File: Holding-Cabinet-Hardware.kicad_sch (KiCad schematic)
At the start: 0 parts

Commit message: Added display circuit
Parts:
- added J1: Conn_02x19_Odd_Even, Connector_PinSocket_2.54mm:PinSocket_2x38_P2.54mm_Vertical, symbol Connector_Generic:Conn_02x19_Odd_Even
- added Q1, Q2, Q3, Q4, Q5, Q6, Q7, Q8: 2N3904, Package_TO_SOT_THT:TO-92_Inline, symbol Transistor_BJT:2N3904
- added Q10, Q11, Q12, Q9: AO3401A, Package_TO_SOT_SMD:SOT-23, symbol Transistor_FET:AO3401A
- added R1, R10, R11, R12, R13, R14, R15, R16, R17, R18, R19, R2, R20, R21, R22, R23, R24, R3, R4, R5, R6, R7, R8, R9: R_US, symbol Device:R_US
- added U1: CC56-12EWA, Display_7Segment:CA56-12EWA, symbol Display_Character:CC56-12EWA
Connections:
- new net: Q1.3 (C), R3.1
- new net: R3.2, U1.11 (a)
- new net: Q10.1 (G), R20.2, R23.1
- new net: Q10.2 (S), U1.6 (CC4)
- new net: Q12.1 (G), R22.1, R24.2
- new net: Q12.2 (S), U1.9 (CC2)
- new net: J1.14 (Pin_14), R18.2
- new net: J1.16 (Pin_16), R22.2
- new net: J1.18 (Pin_18), R21.2
- new net: J1.20 (Pin_20), R23.2
- new net: J1.22 (Pin_22), R1.1
- new net: J1.24 (Pin_24), R2.1
- new net: J1.26 (Pin_26), R5.2
- new net: J1.28 (Pin_28), R7.2
- new net: J1.30 (Pin_30), R9.2
- new net: J1.32 (Pin_32), R11.2
- new net: J1.34 (Pin_34), R13.2
- new net: J1.36 (Pin_36), R15.2
- new net: Q3.2 (B), R5.1
- new net: Q3.3 (C), R6.1
- new net: Q9.1 (G), R17.2, R18.1
- new net: Q8.2 (B), R15.1
- new net: Q9.2 (S), U1.12 (CC1)
- new net: Q7.2 (B), R13.1
- new net: Q7.3 (C), R14.1
- new net: R6.2, U1.4 (c)
- new net: Q4.2 (B), R7.1
- new net: Q4.3 (C), R8.1
- new net: R8.2, U1.2 (d)
- new net: Q5.3 (C), R10.1
- new net: R10.2, U1.1 (e)
- new net: Q11.1 (G), R19.2, R21.1
- new net: Q6.2 (B), R11.1
- new net: Q2.2 (B), R2.2
- new net: Q6.3 (C), R12.1
- new net: Q8.3 (C), R16.1
- new net: Q11.2 (S), U1.8 (CC3)
- new net: R12.2, U1.10 (f)
- new net: R16.2, U1.3 (DPX)
- new net: R14.2, U1.5 (g)
- new net: R4.2, U1.7 (b)
- new net: Q1.2 (B), R1.2
- new net: Q5.2 (B), R9.1
- new net: Q2.3 (C), R4.1
- new net GND: J1.37 (Pin_37), J1.38 (Pin_38), Q1.1 (E), Q2.1 (E), Q3.1 (E), Q4.1 (E), Q5.1 (E), Q6.1 (E), Q7.1 (E), Q8.1 (E)
- new net VCC: J1.1 (Pin_1), J1.2 (Pin_2), Q10.3 (D), Q9.3 (D), R17.1, R19.1, R20.1, R24.1

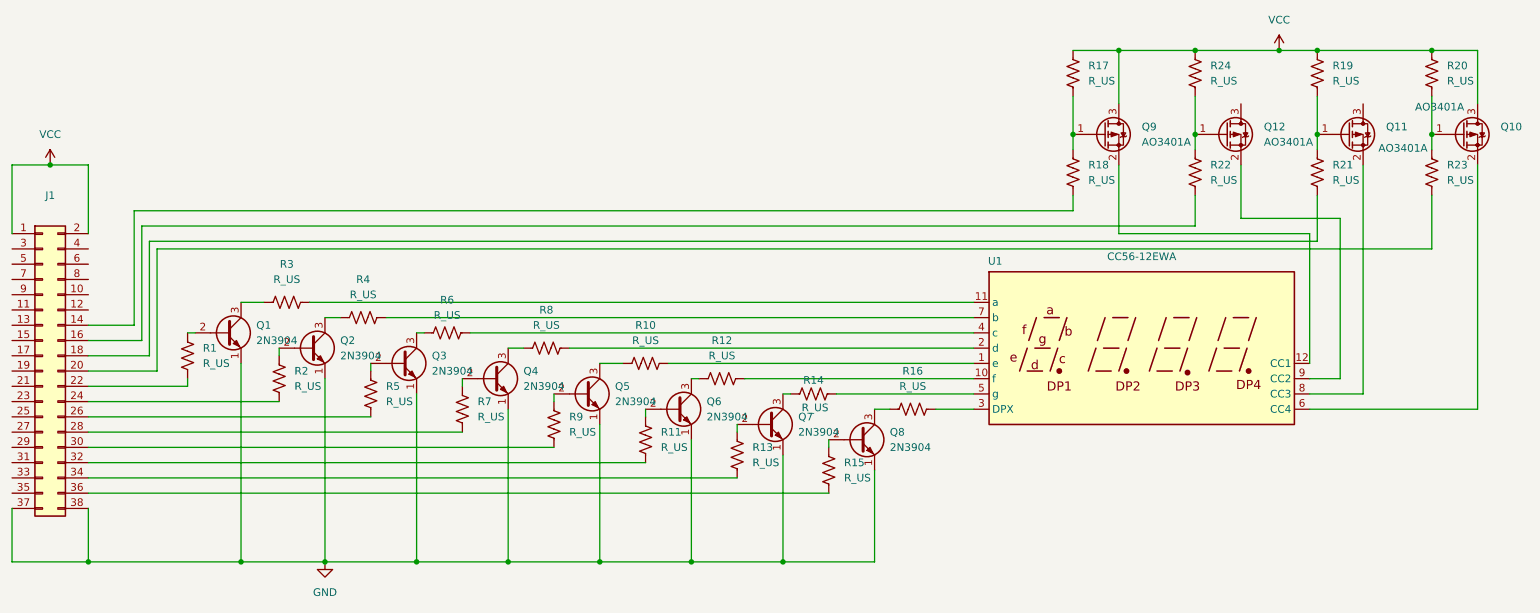
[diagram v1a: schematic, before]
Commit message: Created hierarchical sheet symbols on root sheet. Added the following schematics: Display, Power Supply, Heater, Fan, Sensing, Connectivity
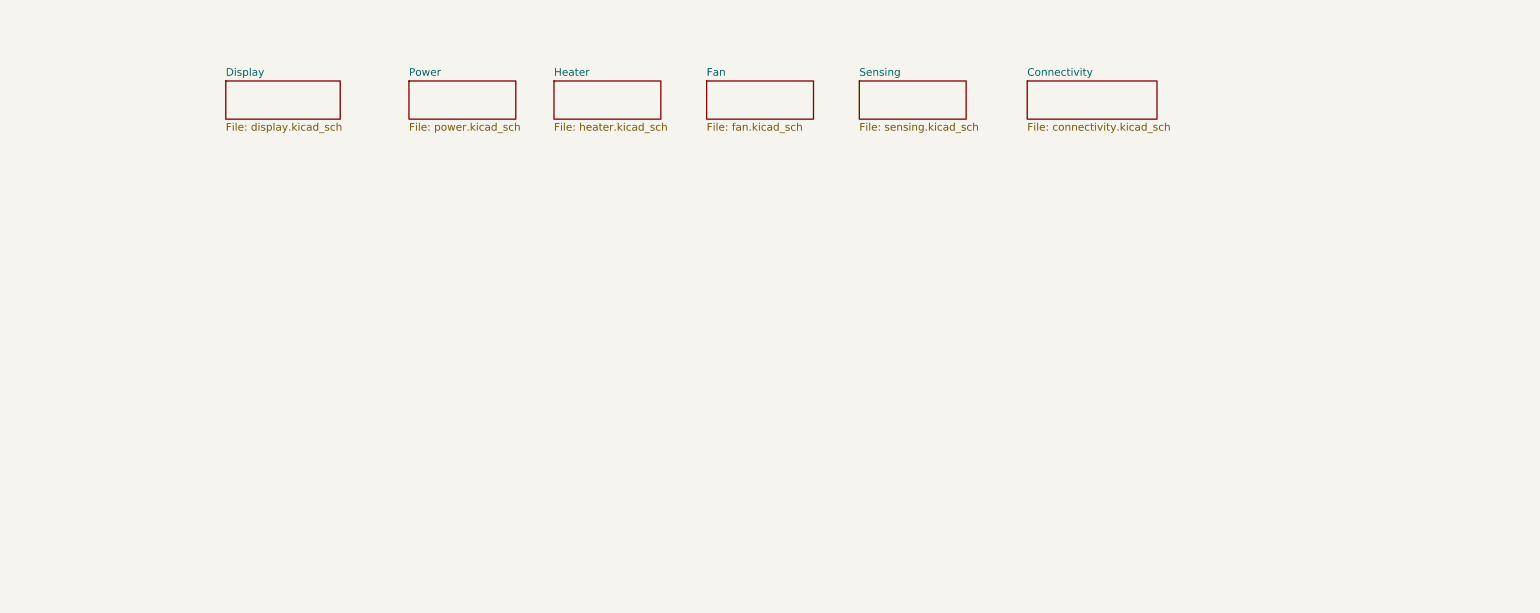
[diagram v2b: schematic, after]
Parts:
- removed J1: Conn_02x19_Odd_Even, Connector_PinSocket_2.54mm:PinSocket_2x38_P2.54mm_Vertical, symbol Connector_Generic:Conn_02x19_Odd_Even
- removed Q1, Q2, Q3, Q4, Q5, Q6, Q7, Q8: 2N3904, Package_TO_SOT_THT:TO-92_Inline, symbol Transistor_BJT:2N3904
- removed Q10, Q11, Q12, Q9: AO3401A, Package_TO_SOT_SMD:SOT-23, symbol Transistor_FET:AO3401A
- removed R1, R10, R11, R12, R13, R14, R15, R16, R17, R18, R19, R2, R20, R21, R22, R23, R24, R3, R4, R5, R6, R7, R8, R9: R_US, symbol Device:R_US
- removed U1: CC56-12EWA, Display_7Segment:CA56-12EWA, symbol Display_Character:CC56-12EWA
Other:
- added sheet Connectivity (connectivity.kicad_sch)
- added sheet Display (display.kicad_sch)
- added sheet Fan (fan.kicad_sch)
- added sheet Heater (heater.kicad_sch)
- added sheet Power (power.kicad_sch)
- added sheet Sensing (sensing.kicad_sch)
- title: Holding Cabinet -> Top Level Sheet 1 of [ ]

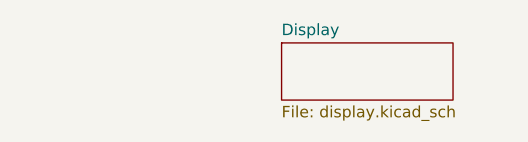
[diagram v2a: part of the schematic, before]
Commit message: Updated the root sheet and added the mcu schematic.
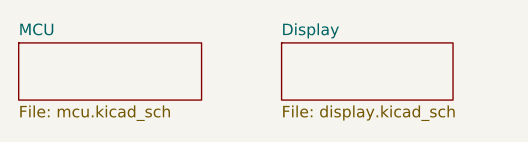
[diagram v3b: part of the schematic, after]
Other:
- added sheet MCU (mcu.kicad_sch)
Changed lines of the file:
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@@
+	)
+	(sheet
+		(at 27.94 58.42)
+		(size 20.32 6.35)
+		(exclude_from_sim no)
+		(in_bom yes)
+		(on_board yes)
+		(dnp no)
+		(fields_autoplaced yes)
+		(stroke
+			(width 0.1524)
+			(type solid)
+		)
+		(fill
+			(color 0 0 0 0)
+		)
+		(property "Sheetname" "MCU"
+			(at 27.94 57.7084 0)
+			(show_name no)
+			(do_not_autoplace no)
+			(effects
+				(font
+					(size 1.27 1.27)
+				)
+				(justify left bottom)
+			)
+		)
+		(property "Sheetfile" "mcu.kicad_sch"
+			(at 27.94 65.3546 0)
+			(show_name no)
+			(do_not_autoplace no)
+			(effects
+				(font
+					(size 1.27 1.27)
+				)
+				(justify left top)
+			)
+		)
+		(instances
+			(project "Holding-Cabinet-Hardware"
+				(path "/a7f4af77-1a94-4795-9d88-0a73c264962c"
+					(page "8")
+				)
+			)
+		)
 	)
 	(sheet

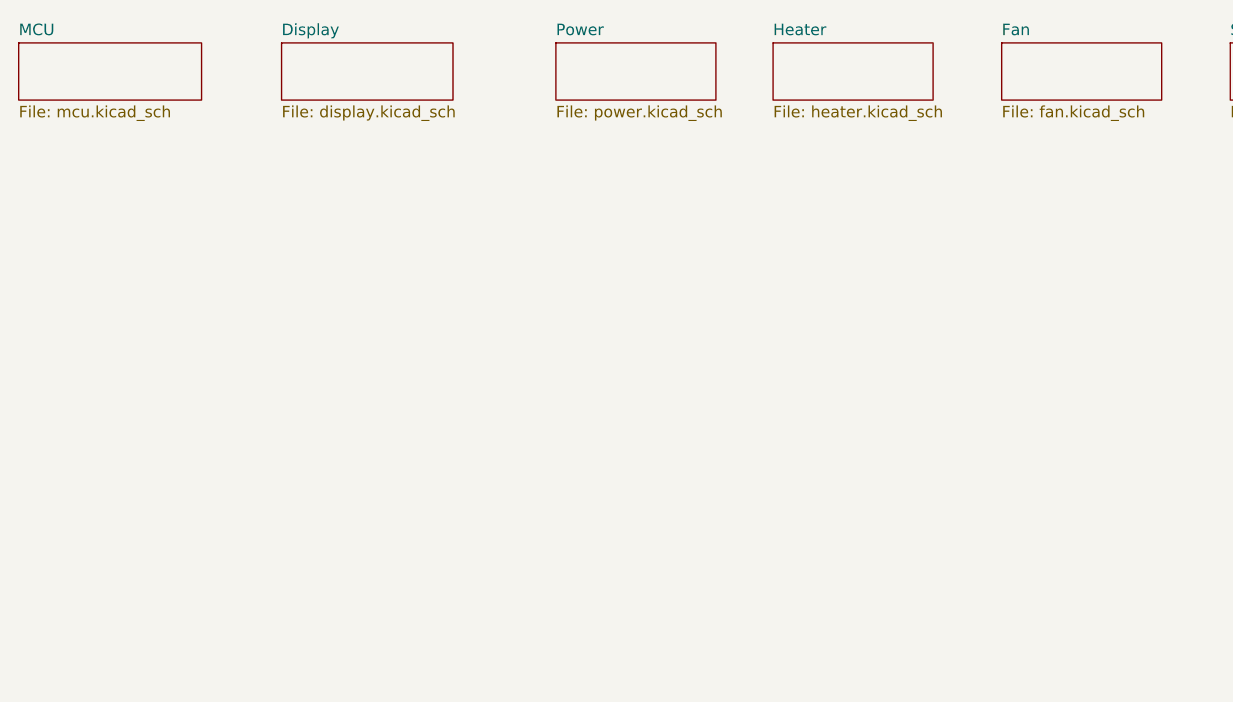
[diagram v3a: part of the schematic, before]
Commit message: Updated sheet connections for MCU to Display
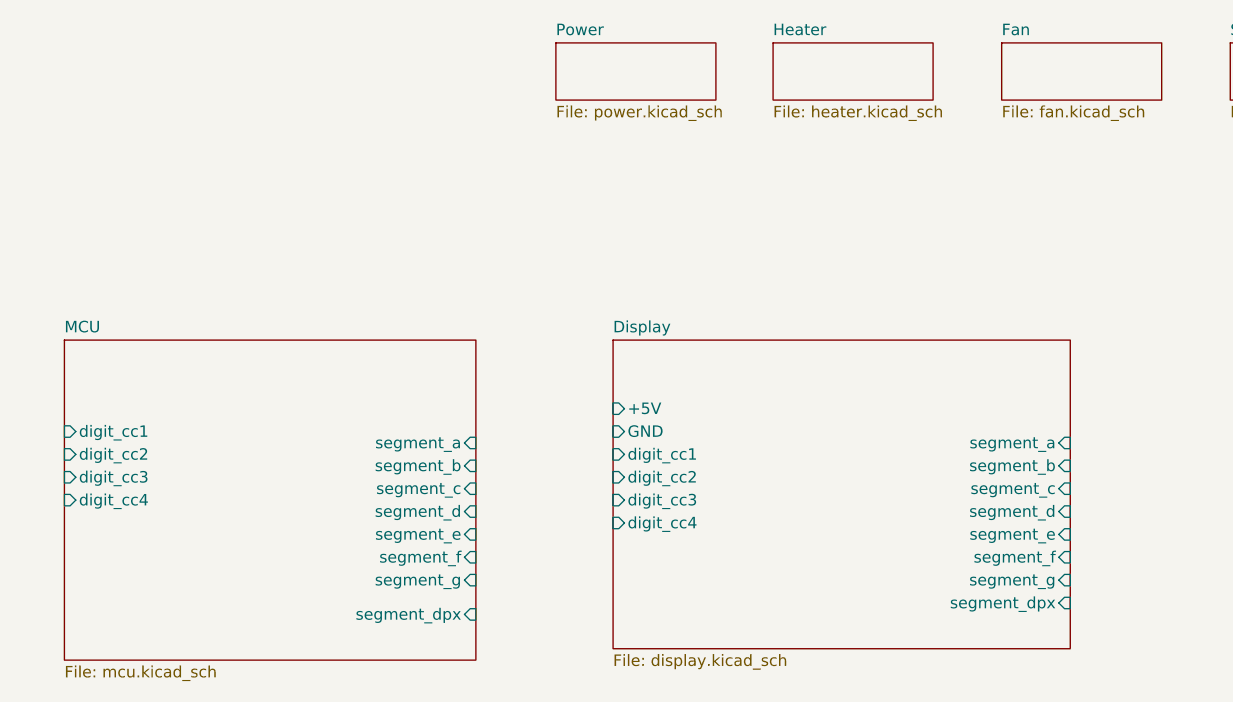
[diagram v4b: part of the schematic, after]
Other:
- sheet Display ports: added +5V, GND, digit_cc1, digit_cc2, digit_cc3, digit_cc4, segment_a, segment_b, segment_c, segment_d, segment_dpx, segment_e, segment_f, segment_g; removed none
- sheet MCU ports: added digit_cc1, digit_cc2, digit_cc3, digit_cc4, segment_a, segment_b, segment_c, segment_d, segment_dpx, segment_e, segment_f, segment_g; removed none

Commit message: Added an LCD
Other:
- sheet Display renamed 7-Segment Display
- added sheet LCD 16x2 Display (lcd_16_2_display.kicad_sch)
- sheet 7-Segment Display: file display.kicad_sch -> 7_segment_display.kicad_sch
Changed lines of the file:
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@@
 			(color 0 0 0 0)
 		)
-		(property "Sheetname" "Display"
+		(property "Sheetname" "7-Segment Display"
 			(at 93.98 90.7284 0)
 			(show_name no)
@@
 			)
 		)
-		(property "Sheetfile" "display.kicad_sch"
+		(property "Sheetfile" "7_segment_display.kicad_sch"
 			(at 93.98 126.3146 0)
 			(show_name no)
@@
 				)
 			)
+		)
+	)
+	(sheet
+		(at 158.75 91.44)
+		(size 57.15 34.29)
+		(exclude_from_sim no)
+		(in_bom yes)
+		(on_board yes)
+		(dnp no)
+		(fields_autoplaced yes)
+		(stroke
+			(width 0.1524)
+			(type solid)
+		)
+		(fill
+			(color 0 0 0 0)
+		)
+		(property "Sheetname" "LCD 16x2 Display"
+			(at 158.75 90.7284 0)
+			(show_name no)
+			(do_not_autoplace no)
+			(effects
+				(font
+					(size 1.27 1.27)
+				)
+				(justify left bottom)
+			)
+		)
+		(property "Sheetfile" "lcd_16_2_display.kicad_sch"
+			(at 158.75 126.3146 0)
+			(show_name no)
+			(do_not_autoplace no)
+			(effects
+				(font
+					(size 1.27 1.27)
+				)
+				(justify left top)
+			)
+		)
+		(instances
+			(project "Holding-Cabinet-Hardware"
+				(path "/a7f4af77-1a94-4795-9d88-0a73c264962c"
+					(page "9")
+				)
+			)

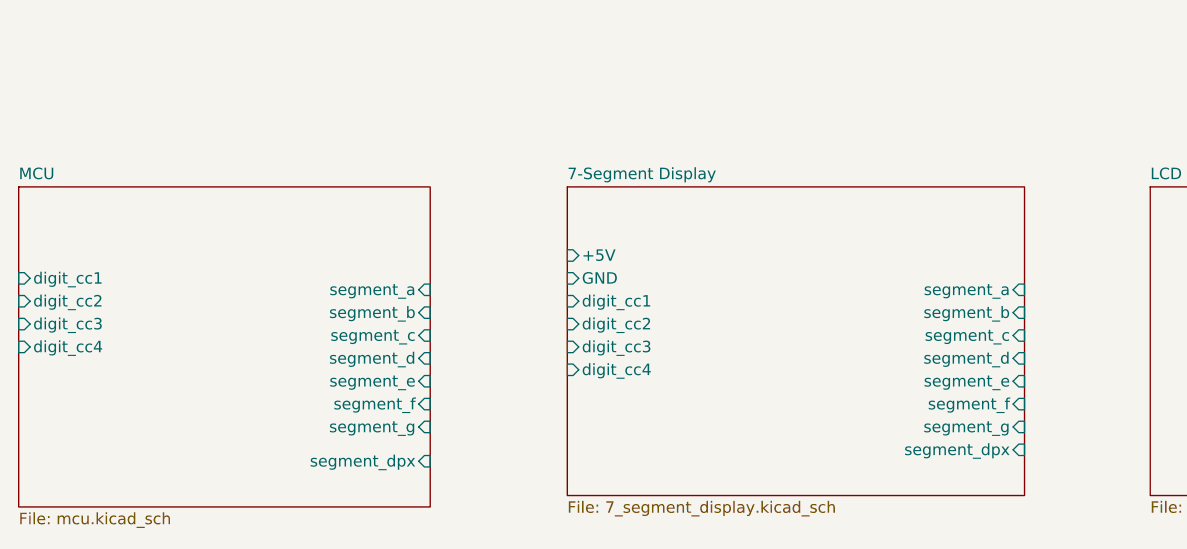
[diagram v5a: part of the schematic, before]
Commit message: Removed the 7 seg display
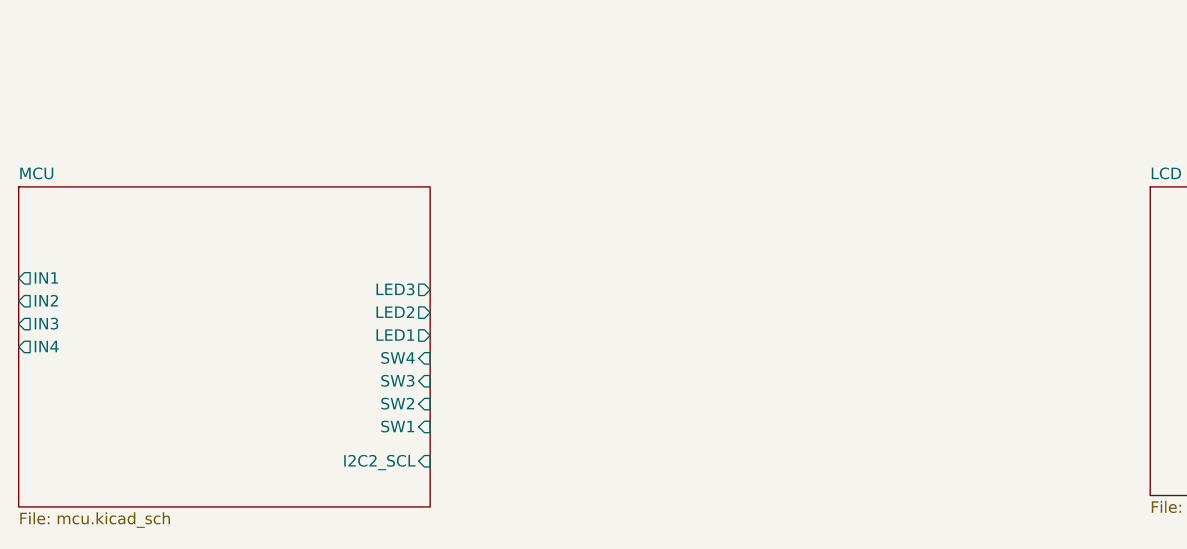
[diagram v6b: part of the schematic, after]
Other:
- removed sheet 7-Segment Display
- sheet MCU ports: added I2C2_SCL, IN1, IN2, IN3, IN4, LED1, LED2, LED3, SW1, SW2, SW3, SW4; removed digit_cc1, digit_cc2, digit_cc3, digit_cc4, segment_a, segment_b, segment_c, segment_d, segment_dpx, segment_e, segment_f, segment_g
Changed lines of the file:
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@@
 			)
 		)
-		(pin "digit_cc1" input
+		(pin "IN1" output
 			(at 33.02 101.6 180)
 			(effects
@@
 			)
 		)
-		(pin "digit_cc2" input
+		(pin "IN2" output
 			(at 33.02 104.14 180)
 			(effects
@@
 			)
 		)
-		(pin "digit_cc3" input
+		(pin "IN3" output
 			(at 33.02 106.68 180)
 			(effects
@@
 			)
 		)
-		(pin "digit_cc4" input
+		(pin "IN4" output
 			(at 33.02 109.22 180)
 			(effects
@@
 			)
 		)
-		(pin "segment_a" input
+		(pin "LED3" output
 			(at 78.74 102.87 0)
 			(effects
@@
 			)
 		)
-		(pin "segment_b" input
+		(pin "LED2" output
 			(at 78.74 105.41 0)
 			(effects
@@
 			)
 		)
-		(pin "segment_c" input
+		(pin "LED1" output
 			(at 78.74 107.95 0)
 			(effects
@@
 			)
 		)
-		(pin "segment_d" input
+		(pin "SW4" input
 			(at 78.74 110.49 0)
 			(effects
@@
 			)
 		)
-		(pin "segment_dpx" input
+		(pin "I2C2_SCL" input
 			(at 78.74 121.92 0)
 			(effects
@@
 			)
 		)
-		(pin "segment_e" input
+		(pin "SW3" input
 			(at 78.74 113.03 0)
 			(effects
@@
 			)
 		)
-		(pin "segment_f" input
+		(pin "SW2" input
 			(at 78.74 115.57 0)
 			(effects
@@
 			)
 		)
-		(pin "segment_g" input
+		(pin "SW1" input
 			(at 78.74 118.11 0)
 			(effects
@@
 				)
 			)
-		)
-	)
-	(sheet
-		(at 93.98 91.44)
-		(size 50.8 34.29)
-		(exclude_from_sim no)
-		(in_bom yes)
-		(on_board yes)
-		(dnp no)
-		(fields_autoplaced yes)
-		(stroke
-			(width 0.1524)
-			(type solid)
-		)
-		(fill
-			(color 0 0 0 0)
-		)
-		(property "Sheetname" "7-Segment Display"
-			(at 93.98 90.7284 0)
-			(show_name no)
-			(do_not_autoplace no)
-			(effects
-				(font
-					(size 1.27 1.27)
-				)
-				(justify left bottom)
-			)
-		)
-		(property "Sheetfile" "7_segment_display.kicad_sch"
-			(at 93.98 126.3146 0)
-			(show_name no)
-			(do_not_autoplace no)
-			(effects
-				(font
-					(size 1.27 1.27)
-				)
-				(justify left top)
-			)
-		)
-		(pin "+5V" input
-			(at 93.98 99.06 180)
-			(effects
-				(font
-					(size 1.27 1.27)
-				)
-				(justify left)
-			)
-		)
-		(pin "digit_cc1" input
-			(at 93.98 104.14 180)
-			(effects
-				(font
-					(size 1.27 1.27)
-				)
-				(justify left)
-			)
-		)
-		(pin "digit_cc2" input
-			(at 93.98 106.68 180)
-			(effects
-				(font
-					(size 1.27 1.27)
-				)
-				(justify left)
-			)
-		)
-		(pin "digit_cc3" input
-			(at 93.98 109.22 180)
-			(effects
-				(font
-					(size 1.27 1.27)
-				)
-				(justify left)
-			)
-		)
-		(pin "digit_cc4" input
-			(at 93.98 111.76 180)
-			(effects
-				(font
-					(size 1.27 1.27)
-				)
-				(justify left)
-			)
-		)
-		(pin "GND" input
-			(at 93.98 101.6 180)
-			(effects
-				(font
-					(size 1.27 1.27)
-				)
-				(justify left)
-			)
-		)
-		(pin "segment_a" input
-			(at 144.78 102.87 0)
-			(effects
-				(font
-					(size 1.27 1.27)
-				)
-				(justify right)
-			)
-		)
-		(pin "segment_b" input
-			(at 144.78 105.41 0)
-			(effects
-				(font
-					(size 1.27 1.27)
-				)
-				(justify right)
-			)
-		)
-		(pin "segment_c" input
-			(at 144.78 107.95 0)
-			(effects
-				(font
-					(size 1.27 1.27)
-				)
-				(justify right)
-			)
-		)
-		(pin "segment_d" input
-			(at 144.78 110.49 0)
-			(effects
-				(font
-					(size 1.27 1.27)
-				)
-				(justify right)
-			)
-		)
-		(pin "segment_dpx" input
-			(at 144.78 120.65 0)
-			(effects
-				(font
-					(size 1.27 1.27)
-				)
-				(justify right)
-			)
-		)
-		(pin "segment_e" input
-			(at 144.78 113.03 0)
-			(effects
-				(font
-					(size 1.27 1.27)
-				)
-				(justify right)
-			)
-		)
-		(pin "segment_f" input
-			(at 144.78 115.57 0)
-			(effects
-				(font
-					(size 1.27 1.27)
-				)
-				(justify right)
-			)
-		)
-		(pin "segment_g" input
-			(at 144.78 118.11 0)
-			(effects
-				(font
-					(size 1.27 1.27)
-				)
-				(justify right)
-			)
-		)
-		(instances
-			(project "Holding-Cabinet-Hardware"
-				(path "/a7f4af77-1a94-4795-9d88-0a73c264962c"
-					(page "2")
-				)
-			)
